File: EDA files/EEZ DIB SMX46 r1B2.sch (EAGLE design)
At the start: 156 parts, among them IC1 STM32F030C6T6, IC2 74HC1G126GW,125, IC3 M24C32-WMN6P, IC4 LP2985-33DBVR, IC5 74HC2G04GW,125, IC6 OPA2170, K1 FTR-C1GA012G-B05, K10 FTR-C1GA012G-B05, K11 FTR-C1GA012G-B05, K12 FTR-C1GA012G-B05, K13 FTR-C1GA012G-B05, K14 FTR-C1GA012G-B05, K15 FTR-C1GA012G-B05, K16 FTR-C1GA012G-B05, K17 FTR-C1GA012G-B05, K18 FTR-C1GA012G-B05, K19 FTR-C1GA012G-B05, K2 FTR-C1GA012G-B05, K20 FTR-C1GA012G-B05, K21 FTR-C1GA012G-B05, K22 FTR-C1GA012G-B05, K23 FTR-C1GA012G-B05, K24 FTR-C1GA012G-B05, K3 FTR-C1GA012G-B05, K4 FTR-C1GA012G-B05, K5 FTR-C1GA012G-B05, K6 FTR-C1GA012G-B05, K7 FTR-C1GA012G-B05, K8 FTR-C1GA012G-B05, K9 FTR-C1GA012G-B05, Q1 2N7002, Q10 2N7002, Q11 2N7002, Q12 2N7002, Q13 2N7002, Q14 2N7002, Q15 2N7002, Q16 2N7002, Q17 2N7002, Q18 2N7002, Q19 2N7002, Q2 2N7002, Q20 2N7002, Q21 2N7002, Q22 2N7002, Q23 2N7002, Q24 2N7002, Q25 2N7002, Q3 2N7002, Q4 2N7002, Q5 2N7002, Q6 2N7002, Q7 2N7002, Q8 2N7002, Q9 2N7002, X1 SSW-106-02-S-S, X2 77317-104-28LF, X3 691327310016, X4 691327310016

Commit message: #1, #2 fixed
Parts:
- C2, C9: device rcl:C-EUC1206 -> rcl:C-EUC0805
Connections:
- net +3V3: now also IC1.VDDA; no longer IC1.VSSA
- net BOOT0: now also X2-26.1
- net GND: now also IC1.VSSA; no longer IC1.VDDA, X2-26.1
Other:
- moved on the sheet: C5, C6, IC2A, RN2-1

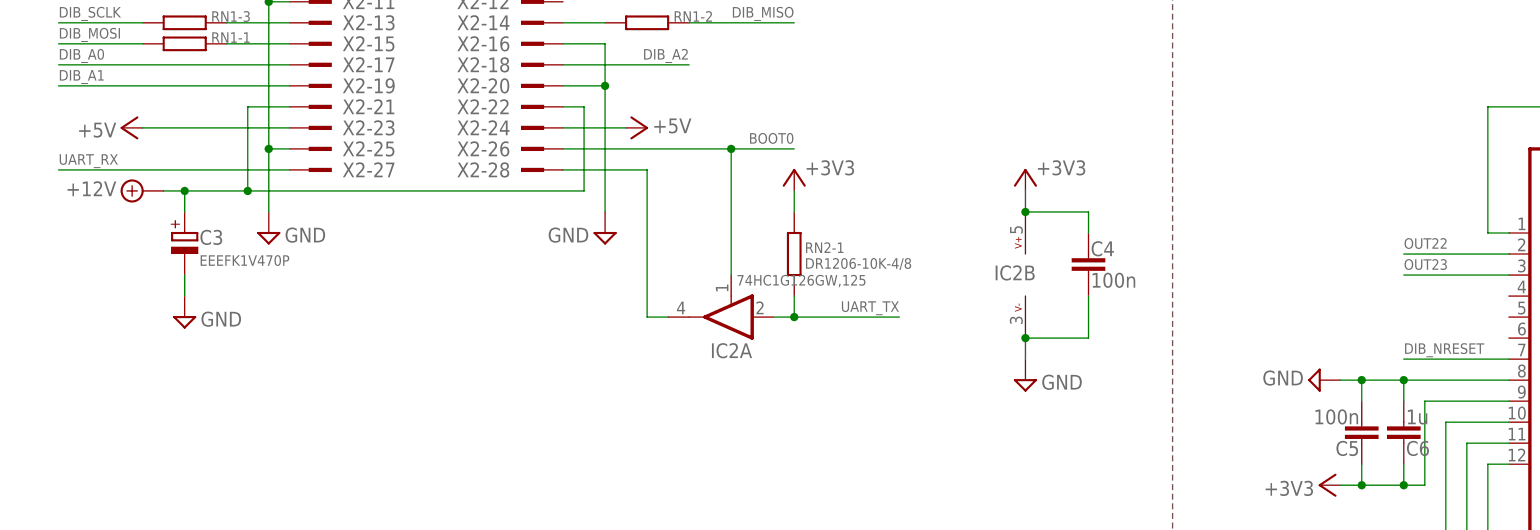
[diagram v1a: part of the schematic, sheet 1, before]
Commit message: swap UART TX and RX
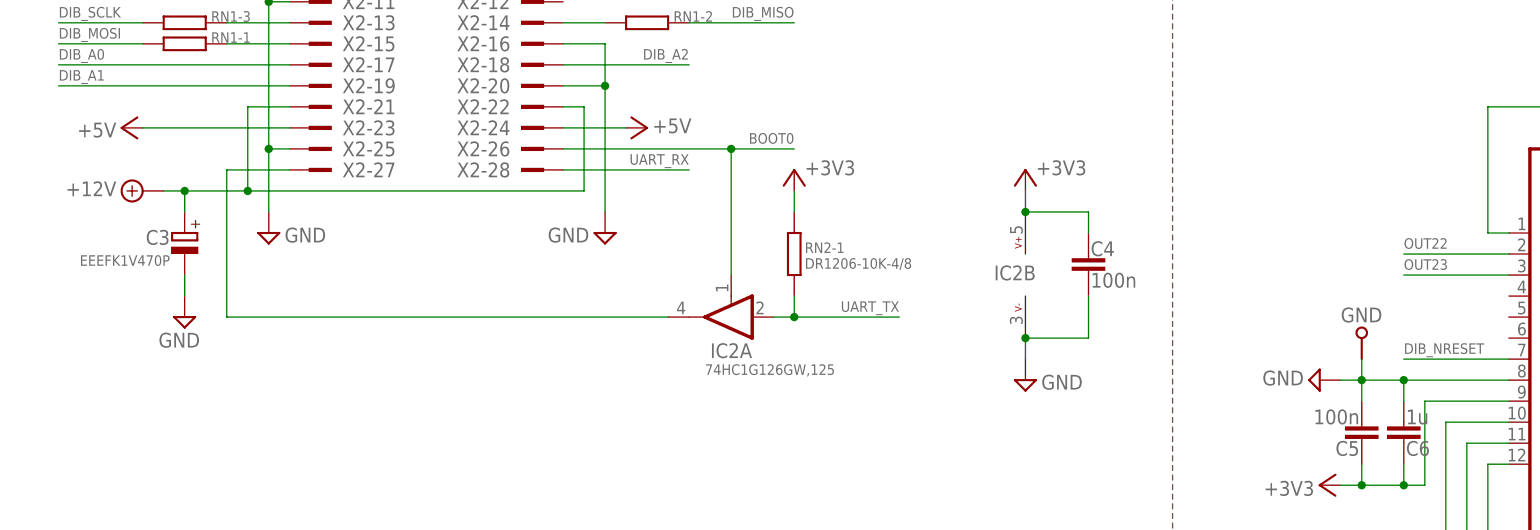
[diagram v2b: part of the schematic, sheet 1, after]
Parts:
- added GND: (no value), EEZ_Lib1:PCB_TEST_TABSHIELD
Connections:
- net GND: now also GND.P$1
- net N$72: now also X2-27.1; no longer X2-28.1
- net UART_RX: now also X2-28.1; no longer X2-27.1
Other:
- note added: "28 UART_TX"
- note added: "UART_RX 27"
- note removed: "28 UART_RX"
- note removed: "UART_TX 27"
- moved on the sheet: C3
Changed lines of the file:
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@@
 <layer number="101" name="Pinouts" color="13" fill="1" visible="yes" active="yes"/>
 <layer number="102" name="Signals" color="3" fill="1" visible="yes" active="yes"/>
+<layer number="103" name="extrainfo" color="5" fill="1" visible="yes" active="yes"/>
+<layer number="104" name="comments" color="9" fill="1" visible="yes" active="yes"/>
 <layer number="105" name="tPlate" color="7" fill="1" visible="no" active="no"/>
 <layer number="106" name="bPlate" color="7" fill="1" visible="no" active="no"/>
@@
 <layer number="111" name="111" color="7" fill="1" visible="no" active="no"/>
 <layer number="112" name="tSilk" color="7" fill="1" visible="no" active="no"/>
+<layer number="114" name="EEZ" color="12" fill="1" visible="yes" active="yes"/>
 <layer number="116" name="Patch_BOT" color="7" fill="1" visible="no" active="no"/>
 <layer number="118" name="Rect_Pads" color="7" fill="1" visible="no" active="no"/>
@@
 <part name="FM1" library="EEZ_Lib1" deviceset="FIDUCIAL" device="_2"/>
 <part name="X1" library="con-samtec" deviceset="SSW-106-02-S-S" device=""/>
+<part name="GND" library="EEZ_Lib1" deviceset="PCB_TEST_TAB" device="SHIELD"/>
 </parts>
 <sheets>
@@
 <circle x="115.57" y="130.81" radius="0.635" width="0.1524" layer="101"/>
 <circle x="118.11" y="130.81" radius="0.635" width="0.1524" layer="101"/>
-<text x="120.65" y="130.175" size="1.4224" layer="101">28 UART_RX</text>
-<text x="113.03" y="131.445" size="1.4224" layer="101" rot="R180">UART_TX 27</text>
+<text x="120.65" y="130.175" size="1.4224" layer="101">28 UART_TX</text>
+<text x="113.03" y="131.445" size="1.4224" layer="101" rot="R180">UART_RX 27</text>
 <text x="7.62" y="63.5" size="1.778" layer="97" rot="MR180">I2C Module ID EEPROM</text>
 <wire x1="142.24" y1="177.8" x2="142.24" y2="154.94" width="0.1524" layer="97" style="shortdash"/>
@@
 <attribute name="VALUE" x="233.68" y="74.93" size="1.778" layer="96" rot="MR180"/>
 </instance>
-<instance part="C3" gate="G$1" x="22.86" y="116.84" smashed="yes">
-<attribute name="NAME" x="24.638" y="115.4176" size="1.778" layer="95"/>
-<attribute name="VALUE" x="24.638" y="112.8776" size="1.27" layer="96"/>
+<instance part="C3" gate="G$1" x="22.86" y="116.84" smashed="yes" rot="MR0">
+<attribute name="NAME" x="21.082" y="115.4176" size="1.778" layer="95" rot="MR0"/>
+<attribute name="VALUE" x="21.082" y="112.8776" size="1.27" layer="96" rot="MR0"/>
 </instance>
 <instance part="SUPPLY45" gate="GND" x="22.86" y="106.68" smashed="yes">
-<attribute name="VALUE" x="24.765" y="107.315" size="1.778" layer="96" rot="MR180"/>
+<attribute name="VALUE" x="19.685" y="104.775" size="1.778" layer="96" rot="MR180"/>
 </instance>
 <instance part="C9" gate="G$1" x="81.28" y="35.56" smashed="yes" rot="R180">
@@
 <instance part="IC2" gate="A" x="88.9" y="106.68" smashed="yes" rot="R180">
 <attribute name="NAME" x="91.44" y="103.505" size="1.778" layer="95" rot="R180"/>
-<attribute name="VALUE" x="89.535" y="111.76" size="1.27" layer="96" rot="MR180"/>
+<attribute name="VALUE" x="85.725" y="100.965" size="1.27" layer="96" rot="MR180"/>
 </instance>
 <instance part="IC2" gate="B" x="124.46" y="111.76" smashed="yes" rot="MR0">
@@
 <instance part="X1" gate="-4" x="177.8" y="165.1" smashed="yes" rot="MR0">
 <attribute name="NAME" x="180.848" y="165.862" size="1.524" layer="95" rot="MR180"/>
+</instance>
+<instance part="GND" gate="G$1" x="165.1" y="104.14" smashed="yes" rot="R90">
+<attribute name="NAME" x="162.56" y="106.045" size="1.778" layer="95"/>
+<attribute name="VALUE" x="167.64" y="104.14" size="1.778" layer="96" rot="R90"/>
 </instance>
 </instances>
@@
 <segment>
 <pinref part="C3" gate="G$1" pin="-"/>
+<pinref part="SUPPLY45" gate="GND" pin="GND"/>
 <wire x1="22.86" y1="111.76" x2="22.86" y2="109.22" width="0.1524" layer="91"/>
-<pinref part="SUPPLY45" gate="GND" pin="GND"/>
 </segment>
 <segment>
@@
 <wire x1="165.1" y1="99.06" x2="162.56" y2="99.06" width="0.1524" layer="91"/>
 <junction x="165.1" y="99.06"/>
+<pinref part="GND" gate="G$1" pin="P$1"/>
+<wire x1="165.1" y1="101.6" x2="165.1" y2="99.06" width="0.1524" layer="91"/>
 </segment>
 </net>
@@
 </segment>
 <segment>
-<pinref part="X2" gate="-27" pin="1"/>
-<wire x1="35.56" y1="124.46" x2="7.62" y2="124.46" width="0.1524" layer="91"/>
-<label x="7.62" y="125.095" size="1.27" layer="102"/>
+<pinref part="X2" gate="-28" pin="1"/>
+<wire x1="68.58" y1="124.46" x2="83.82" y2="124.46" width="0.1524" layer="91"/>
+<label x="83.82" y="125.095" size="1.27" layer="102" rot="MR0"/>
 </segment>
 </net>
@@
 <net name="N$72" class="0">
 <segment>
-<pinref part="X2" gate="-28" pin="1"/>
-<wire x1="68.58" y1="124.46" x2="78.74" y2="124.46" width="0.1524" layer="91"/>
-<wire x1="78.74" y1="124.46" x2="78.74" y2="106.68" width="0.1524" layer="91"/>
-<wire x1="78.74" y1="106.68" x2="81.28" y2="106.68" width="0.1524" layer="91"/>
 <pinref part="IC2" gate="A" pin="O"/>
-</segment>
-</net>
+<wire x1="81.28" y1="106.68" x2="27.94" y2="106.68" width="0.1524" layer="91"/>
+<wire x1="27.94" y1="106.68" x2="27.94" y2="124.46" width="0.1524" layer="91"/>
+<pinref part="X2" gate="-27" pin="1"/>
+<wire x1="27.94" y1="124.46" x2="35.56" y2="124.46" width="0.1524" layer="91"/>
+</segment>
+</net>

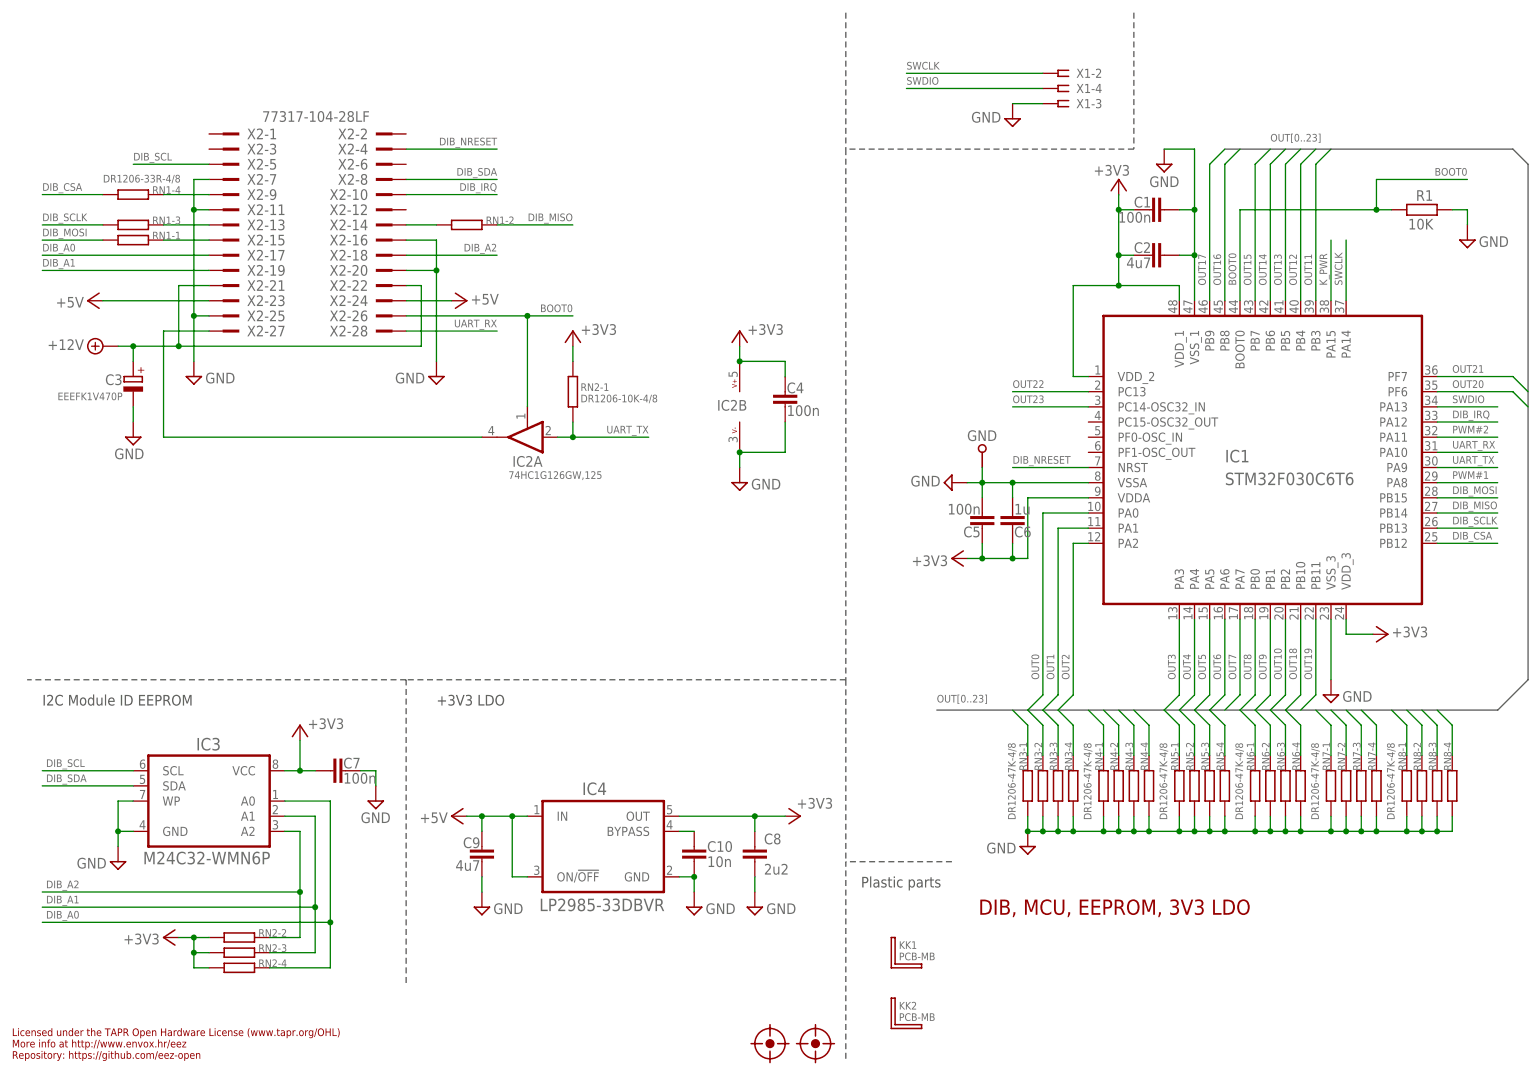
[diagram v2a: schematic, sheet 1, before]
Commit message: DIB alternative IRQs added
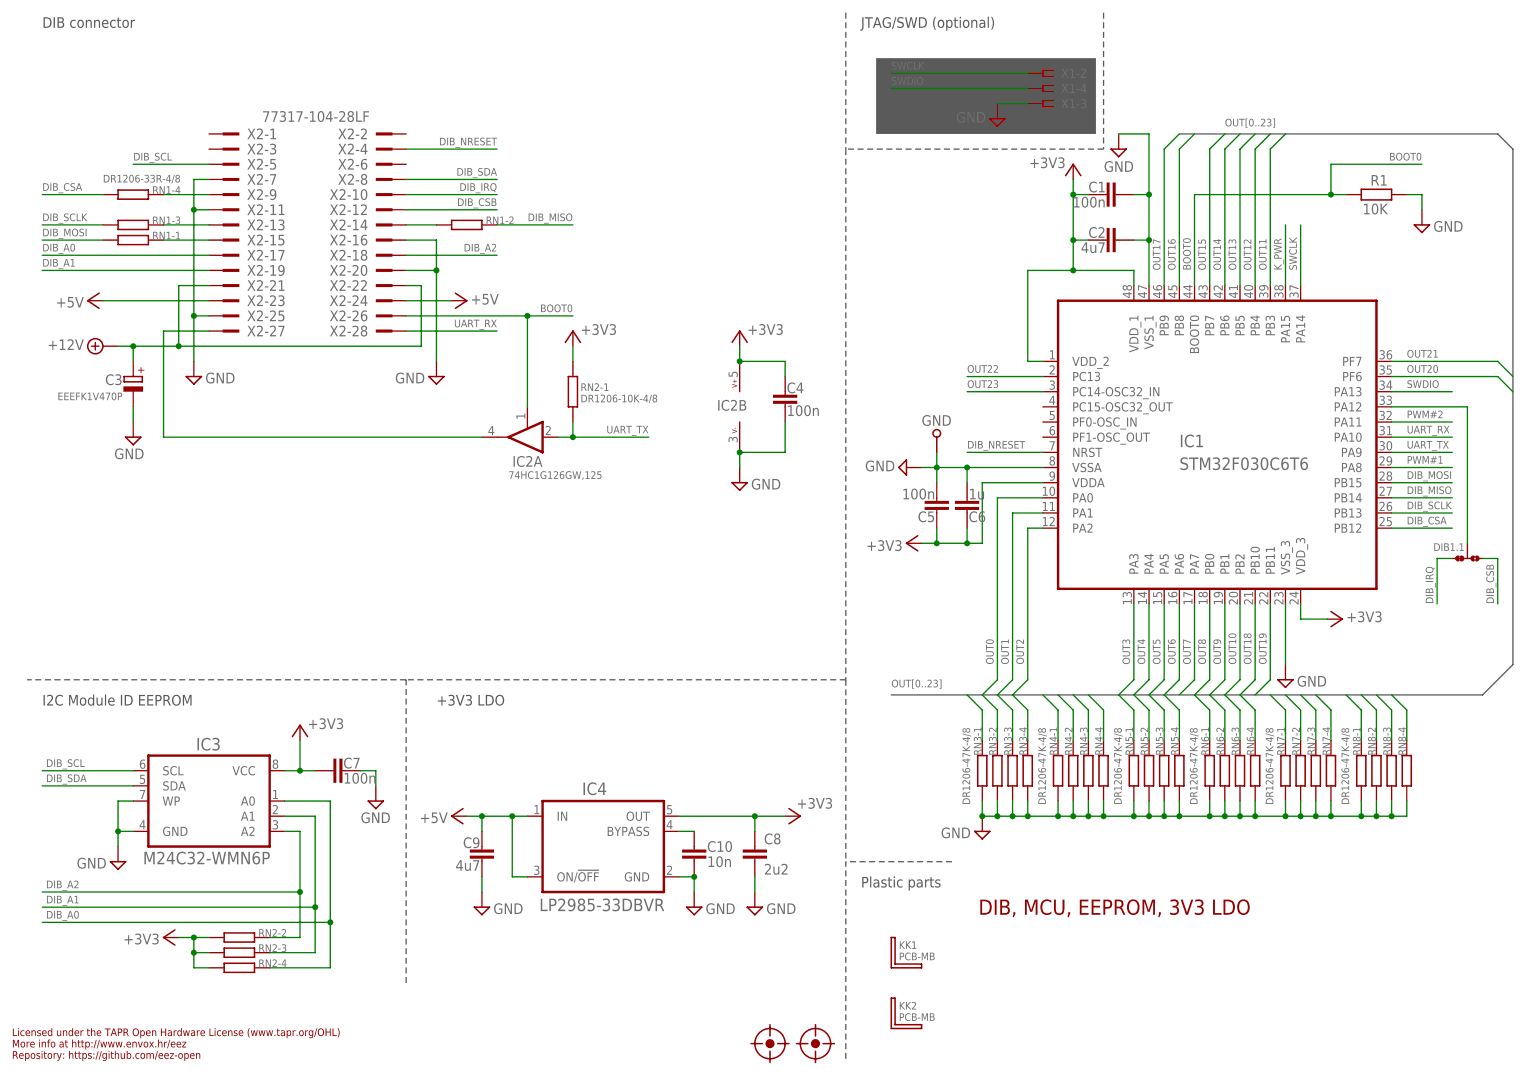
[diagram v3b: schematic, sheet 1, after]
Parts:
- added DIB1.1: JP3-CUT-0805-ROTATED, EEZ_Lib1:JP3-CUT-0805-ROTATED
- X1: value SSW-106-02-S-S -> N.C.
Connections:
- new net DIB_CSB: DIB1.1.NO, X2-12.1
- new net N$75: DIB1.1.COM, IC1.PA12
- net DIB_IRQ: now also DIB1.1.NC; no longer IC1.PA12
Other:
- note added: "DIB connector"
- note added: "JTAG/SWD (optional)"
- moved on the sheet: C1, C2, C5, C6, GND, IC1, R1, RN3-1, RN3-2, RN3-3, RN3-4, RN4-1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
